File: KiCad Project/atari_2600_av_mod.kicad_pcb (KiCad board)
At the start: 2 copper layers, 52 x 28 mm, 20 parts, among them J1 INPUT, J2 OUTPUT, J3 Conn_01x01_Pin, J4 Conn_01x01_Pin, J5 Conn_01x01_Pin, J6 Conn_01x01_Pin, Q1 2SC1815, U1 4050

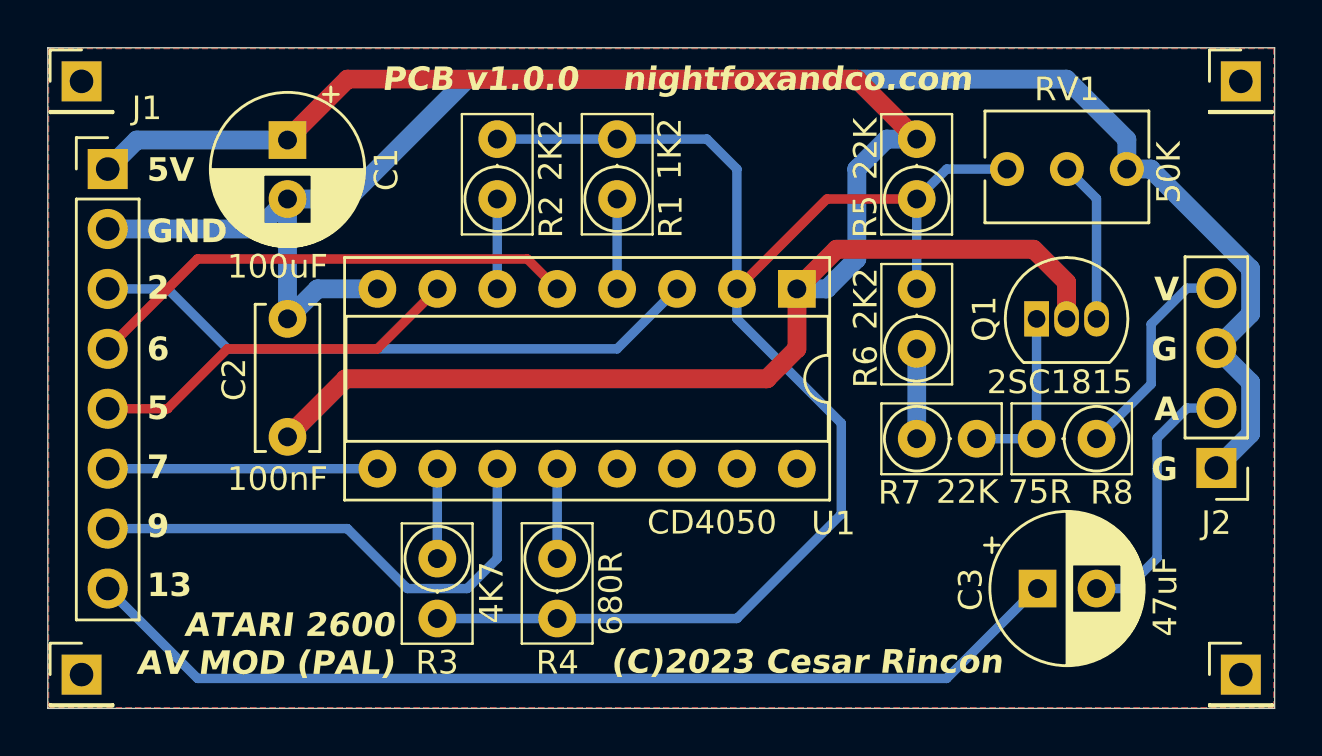
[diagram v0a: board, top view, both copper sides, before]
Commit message: v1.1.0
- Updated 2SC1815 footprint.
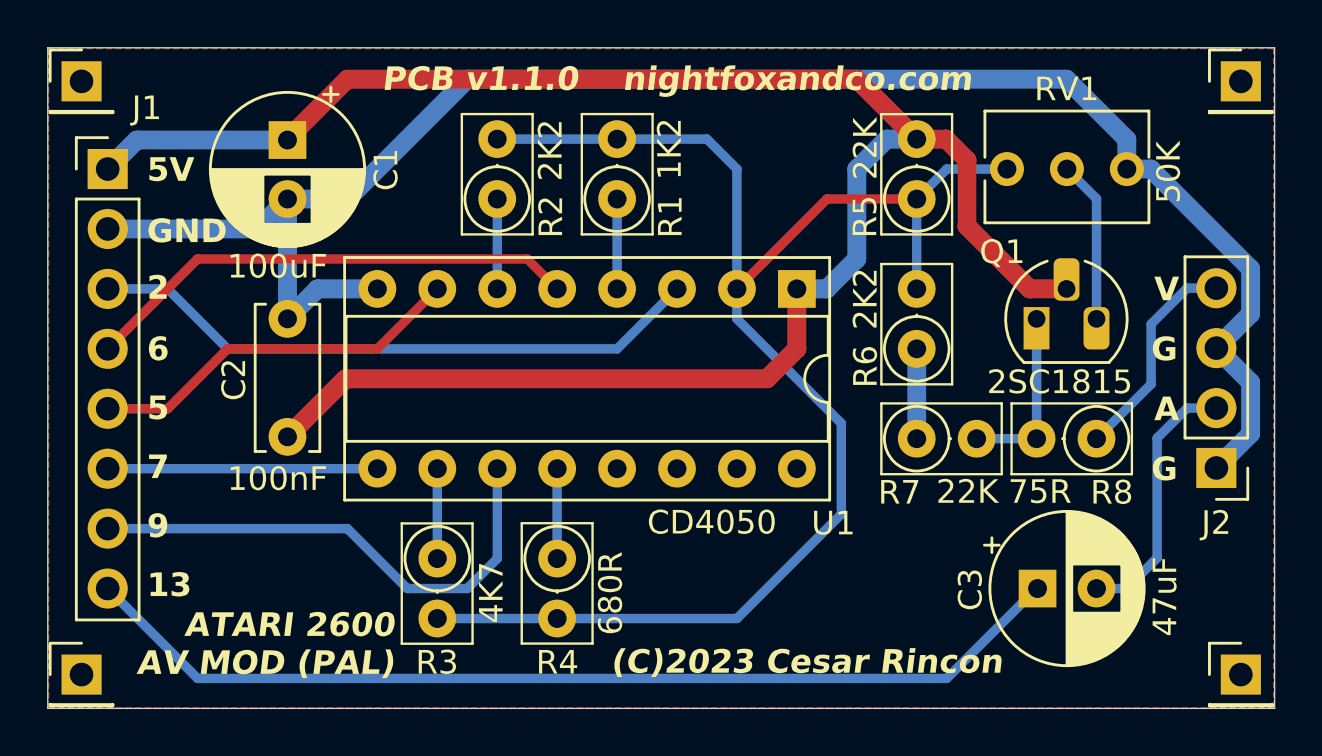
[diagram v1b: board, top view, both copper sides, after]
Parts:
- Q1: footprint Package_TO_SOT_THT:TO-92_Inline -> Package_TO_SOT_THT:TO-92_HandSolder
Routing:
- net /+5V: track 86.8 -> 83.1 mm
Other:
- board text added: "PCB v1.1.0"
- board text removed: "PCB v1.0.0"
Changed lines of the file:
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@@
       (stroke (width 0.1) (type solid)) (layer "F.Fab"))
     (pad "1" thru_hole rect (at 0 0) (size 1.7 1.7) (drill 1) (layers "*.Cu" "*.Mask")
-      (net 2 "/GND") (pinfunction "Pin_1") (pintype "passive+no_connect"))
+      (net 2 "/GND") (pinfunction "Pin_1") (pintype "passive"))
     (model "${KICAD6_3DMODEL_DIR}/Connector_PinHeader_2.54mm.3dshapes/PinHeader_1x01_P2.54mm_Vertical.wrl"
       (offset (xyz 0 0 0))
@@
       (stroke (width 0.1) (type solid)) (layer "F.Fab"))
     (pad "1" thru_hole rect (at 0 0) (size 1.7 1.7) (drill 1) (layers "*.Cu" "*.Mask")
-      (net 2 "/GND") (pinfunction "Pin_1") (pintype "passive+no_connect"))
+      (net 2 "/GND") (pinfunction "Pin_1") (pintype "passive"))
     (model "${KICAD6_3DMODEL_DIR}/Connector_PinHeader_2.54mm.3dshapes/PinHeader_1x01_P2.54mm_Vertical.wrl"
       (offset (xyz 0 0 0))
@@
     )
   )
-  (footprint "Package_TO_SOT_THT:TO-92_Inline" (layer "F.Cu")
+  (footprint "Package_TO_SOT_THT:TO-92_HandSolder" (layer "F.Cu")
     (at 55.85 25.43)
-    (descr "TO-92 leads in-line, narrow, oval pads, drill 0.75mm (see NXP sot054_po.pdf)")
+    (descr "TO-92 leads molded, narrow, drill 0.75mm, handsoldering variant with enlarged pads (see NXP sot054_po.pdf)")
     (tags "to-92 sc-43 sc-43a sot54 PA33 transistor")
     (property "Sheetfile" "atari_2600_av_mod.kicad_sch")
@@
     (property "ki_keywords" "Low Noise Audio NPN Transistor")
     (attr through_hole)
-    (fp_text reference "Q1" (at -2.21 0 90) (layer "F.SilkS")
+    (fp_text reference "Q1" (at -1.45 -2.83) (layer "F.SilkS")
         (effects (font (size 1 1) (thickness 0.15)))
     )
@@
     (fp_line (start -0.53 1.85) (end 3.07 1.85)
       (stroke (width 0.12) (type solid)) (layer "F.SilkS"))
-    (fp_arc (start -0.568478 1.838478) (mid -1.132087 -0.994977) (end 1.27 -2.6)
-      (stroke (width 0.12) (type solid)) (layer "F.SilkS"))
-    (fp_arc (start 1.27 -2.6) (mid 3.672087 -0.994977) (end 3.108478 1.838478)
-      (stroke (width 0.12) (type solid)) (layer "F.SilkS"))
-    (fp_line (start -1.46 -2.73) (end -1.46 2.01)
-      (stroke (width 0.05) (type solid)) (layer "F.CrtYd"))
-    (fp_line (start -1.46 -2.73) (end 4 -2.73)
+    (fp_arc (start -0.541875 1.841741) (mid -1.247231 -0.581764) (end 0.45 -2.45)
+      (stroke (width 0.12) (type solid)) (layer "F.SilkS"))
+    (fp_arc (start 2.05 -2.45) (mid 3.769931 -0.601036) (end 3.078445 1.827684)
+      (stroke (width 0.12) (type solid)) (layer "F.SilkS"))
+    (fp_line (start -1.46 -3.05) (end -1.46 2.01)
+      (stroke (width 0.05) (type solid)) (layer "F.CrtYd"))
+    (fp_line (start -1.46 -3.05) (end 4 -3.05)
       (stroke (width 0.05) (type solid)) (layer "F.CrtYd"))
     (fp_line (start 4 2.01) (end -1.46 2.01)
       (stroke (width 0.05) (type solid)) (layer "F.CrtYd"))
-    (fp_line (start 4 2.01) (end 4 -2.73)
+    (fp_line (start 4 2.01) (end 4 -3.05)
       (stroke (width 0.05) (type solid)) (layer "F.CrtYd"))
     (fp_line (start -0.5 1.75) (end 3 1.75)
@@
     (fp_arc (start 1.27 -2.48) (mid 3.561221 -0.949055) (end 3.023625 1.753625)
       (stroke (width 0.1) (type solid)) (layer "F.Fab"))
-    (pad "1" thru_hole rect (at 0 0) (size 1.05 1.5) (drill 0.75) (layers "*.Cu" "*.Mask")
+    (pad "1" thru_hole rect (at 0 0) (size 1.1 1.8) (drill 0.75 (offset 0 0.4)) (layers "*.Cu" "*.Mask")
       (net 3 "Net-(Q1-E)") (pinfunction "E") (pintype "passive"))
-    (pad "2" thru_hole oval (at 1.27 0) (size 1.05 1.5) (drill 0.75) (layers "*.Cu" "*.Mask")
+    (pad "2" thru_hole roundrect (at 1.27 -1.27) (size 1.1 1.8) (drill 0.75 (offset 0 -0.4)) (layers "*.Cu" "*.Mask") (roundrect_rratio 0.25)
       (net 1 "/+5V") (pinfunction "C") (pintype "passive"))
-    (pad "3" thru_hole oval (at 2.54 0) (size 1.05 1.5) (drill 0.75) (layers "*.Cu" "*.Mask")
+    (pad "3" thru_hole roundrect (at 2.54 0) (size 1.1 1.8) (drill 0.75 (offset 0 0.4)) (layers "*.Cu" "*.Mask") (roundrect_rratio 0.25)
       (net 4 "Net-(Q1-B)") (pinfunction "B") (pintype "input"))
-    (model "${KICAD6_3DMODEL_DIR}/Package_TO_SOT_THT.3dshapes/TO-92_Inline.wrl"
+    (model "${KICAD6_3DMODEL_DIR}/Package_TO_SOT_THT.3dshapes/TO-92.wrl"
       (offset (xyz 0 0 0))
       (scale (xyz 1 1 1))
@@
       (stroke (width 0.1) (type solid)) (layer "F.Fab"))
     (pad "1" thru_hole rect (at 0 0) (size 1.7 1.7) (drill 1) (layers "*.Cu" "*.Mask")
-      (net 2 "/GND") (pinfunction "Pin_1") (pintype "passive+no_connect"))
+      (net 2 "/GND") (pinfunction "Pin_1") (pintype "passive"))
     (model "${KICAD6_3DMODEL_DIR}/Connector_PinHeader_2.54mm.3dshapes/PinHeader_1x01_P2.54mm_Vertical.wrl"
       (offset (xyz 0 0 0))
@@
       (stroke (width 0.1) (type solid)) (layer "F.Fab"))
     (pad "1" thru_hole rect (at 0 0) (size 1.7 1.7) (drill 1) (layers "*.Cu" "*.Mask")
-      (net 2 "/GND") (pinfunction "Pin_1") (pintype "passive+no_connect"))
+      (net 2 "/GND") (pinfunction "Pin_1") (pintype "passive"))
     (model "${KICAD6_3DMODEL_DIR}/Connector_PinHeader_2.54mm.3dshapes/PinHeader_1x01_P2.54mm_Vertical.wrl"
       (offset (xyz 0 0 0))
@@
     (effects (font (size 1 1) (thickness 0.2) bold) (justify left bottom))
   )
-  (gr_text "PCB v1.0.0" (at 28.09 15.85) (layer "F.SilkS")
+  (gr_text "PCB v1.1.0" (at 28.09 15.85) (layer "F.SilkS")
     (effects (font (size 1 1) (thickness 0.2) bold italic) (justify left bottom))
   )
@@
     (effects (font (size 1 1) (thickness 0.1)) (justify left bottom))
   )
+  (segment (start 50.77 17.81) (end 52.01 17.81) (width 0.8) (layer "F.Cu") (net 1))
   (segment (start 26.64 15.27) (end 48.23 15.27) (width 0.8) (layer "F.Cu") (net 1))
+  (segment (start 55.56 24.16) (end 57.12 24.16) (width 0.8) (layer "F.Cu") (net 1))
   (segment (start 44.42 27.97) (end 45.69 26.7) (width 0.8) (layer "F.Cu") (net 1))
-  (segment (start 47.371 22.479) (end 45.69 24.16) (width 0.8) (layer "F.Cu") (net 1))
-  (segment (start 55.719 22.479) (end 47.371 22.479) (width 0.8) (layer "F.Cu") (net 1))
   (segment (start 24.1 30.43) (end 26.56 27.97) (width 0.8) (layer "F.Cu") (net 1))
-  (segment (start 57.12 25.43) (end 57.12 23.88) (width 0.8) (layer "F.Cu") (net 1))
   (segment (start 24.1 17.81) (end 26.64 15.27) (width 0.8) (layer "F.Cu") (net 1))
+  (segment (start 52.9 21.5) (end 55.56 24.16) (width 0.8) (layer "F.Cu") (net 1))
   (segment (start 26.56 27.97) (end 44.42 27.97) (width 0.8) (layer "F.Cu") (net 1))
   (segment (start 45.69 26.7) (end 45.69 24.16) (width 0.8) (layer "F.Cu") (net 1))
-  (segment (start 57.12 23.88) (end 55.719 22.479) (width 0.8) (layer "F.Cu") (net 1))
+  (segment (start 52.01 17.81) (end 52.9 18.7) (width 0.8) (layer "F.Cu") (net 1))
   (segment (start 48.23 15.27) (end 50.77 17.81) (width 0.8) (layer "F.Cu") (net 1))
+  (segment (start 52.9 18.7) (end 52.9 21.5) (width 0.8) (layer "F.Cu") (net 1))
   (segment (start 50.77 17.81) (end 49.5 17.81) (width 0.8) (layer "B.Cu") (net 1))
   (segment (start 49.5 17.81) (end 48.23 19.08) (width 0.8) (layer "B.Cu") (net 1))
